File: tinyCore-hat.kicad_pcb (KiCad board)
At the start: 4 copper layers, 49 x 47.5 mm, 3 parts, among them J2 PPTC081LFBN-RC, J3 PPTC081LFBN-RC, J4 HTSW-109-07-X-SJ

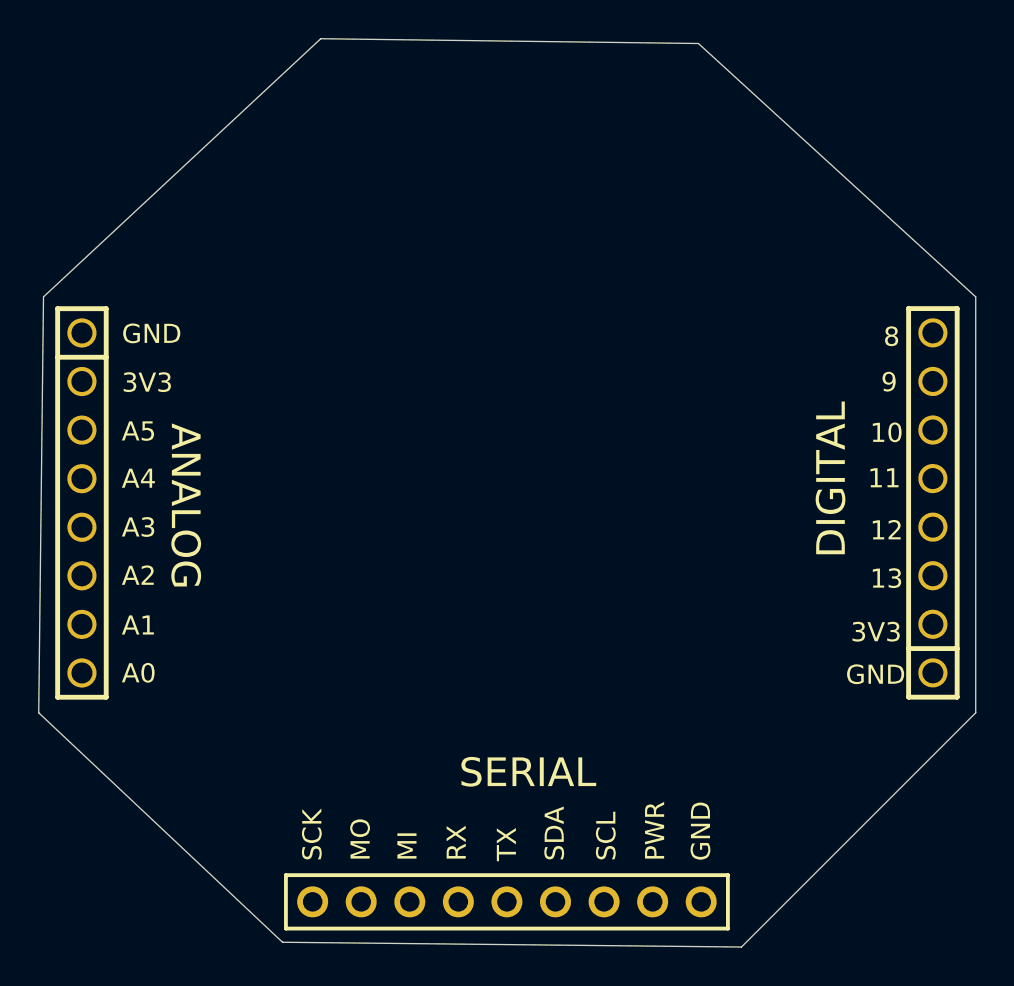
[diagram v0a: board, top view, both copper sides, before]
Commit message: fix(pcb): gnd plane
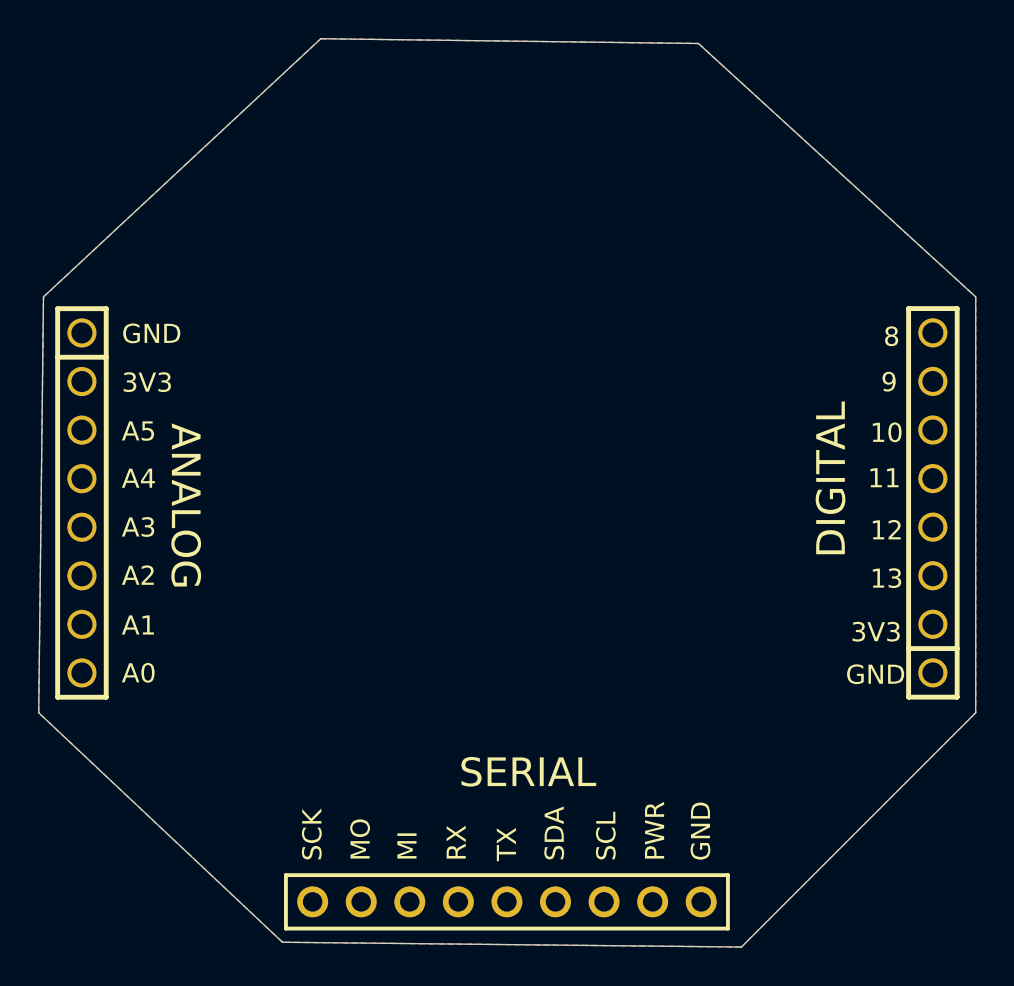
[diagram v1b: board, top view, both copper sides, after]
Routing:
- added copper zone on B.Cu, net GND
- added copper zone on F.Cu, net GND
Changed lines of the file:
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@@
 		(property ki_fp_filters "*8_PIN_100MIL - Female*")
 		(sheetname "/")
-		(sheetfile "tinyCore.kicad_sch")
+		(sheetfile "tinyCore-hat.kicad_sch")
 		(fp_line
 			(start -1.27 1.27)
@@
 		(property ki_fp_filters "*JM-9_HTSW-109-07-X-S*")
 		(sheetname "/")
-		(sheetfile "tinyCore.kicad_sch")
+		(sheetfile "tinyCore-hat.kicad_sch")
 		(fp_circle
 			(center -10.16 0)
@@
 		(property ki_fp_filters "*8_PIN_100MIL - Female*")
 		(sheetname "/")
-		(sheetfile "tinyCore.kicad_sch")
+		(sheetfile "tinyCore-hat.kicad_sch")
 		(fp_line
 			(start 19.05 -1.27)
@@
 		(net 22)
 		(net_name "GND")
+		(layer "F.Cu")
+		(hatch edge 0.5)
+		(priority 1)
+		(connect_pads
+			(clearance 0.5)
+		)
+		(min_thickness 0.25)
+		(filled_areas_thickness no)
+		(fill yes
+			(thermal_gap 0.5)
+			(thermal_bridge_width 0.5)
+		)
+		(polygon
+			(pts
+				(xy 138.75 80.75) (xy 158.5 81) (xy 173 94.25) (xy 173 116) (xy 160.75 128.25) (xy 136.75 128) (xy 124 116)
+				(xy 124.25 94.25)
+			)
+		)
+	)
+	(zone
+		(net 22)
+		(net_name "GND")
+		(layer "B.Cu")
+		(hatch edge 0.5)
+		(priority 2)
+		(connect_pads
+			(clearance 0.5)
+		)
+		(min_thickness 0.25)
+		(filled_areas_thickness no)
+		(fill yes
+			(thermal_gap 0.5)
+			(thermal_bridge_width 0.5)
+		)
+		(polygon
+			(pts
+				(xy 138.75 80.75) (xy 158.5 81) (xy 173 94.25) (xy 173 116) (xy 160.75 128.25) (xy 136.75 128) (xy 124 116)
+				(xy 124.25 94.25)
+			)
+		)
+	)
+	(zone
+		(net 22)
+		(net_name "GND")
 		(layer "In1.Cu")
 		(hatch edge 0.5)
@@
 		(min_thickness 0.25)
 		(filled_areas_thickness no)
-		(fill
+		(fill yes
 			(thermal_gap 0.254)
 			(thermal_bridge_width 0.254)
@@
 		(min_thickness 0.25)
 		(filled_areas_thickness no)
-		(fill
+		(fill yes
 			(thermal_gap 0.254)
 			(thermal_bridge_width 0.254)
